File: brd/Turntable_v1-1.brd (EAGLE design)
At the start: 100 x 80 mm, 117 parts, among them CON1 Pannel, CON2 CAN, CON3 Turntable, CON4 STEPPER_CON, CON5 STEPPER_CON, CON8 SPK, IC1 7805, IC2 LM393N, J1 MiniStp2, J10 MiniStp1, Q1 BS170, SW1 EC12E_SW, U2 LED NANO, X1 AK500/2+M, X2 AK500/2+M, X3 MAB 5SH Conrad: 738247 - VQ, X4 AK500/2+M, X5 Reichelt MEBP 8-8S

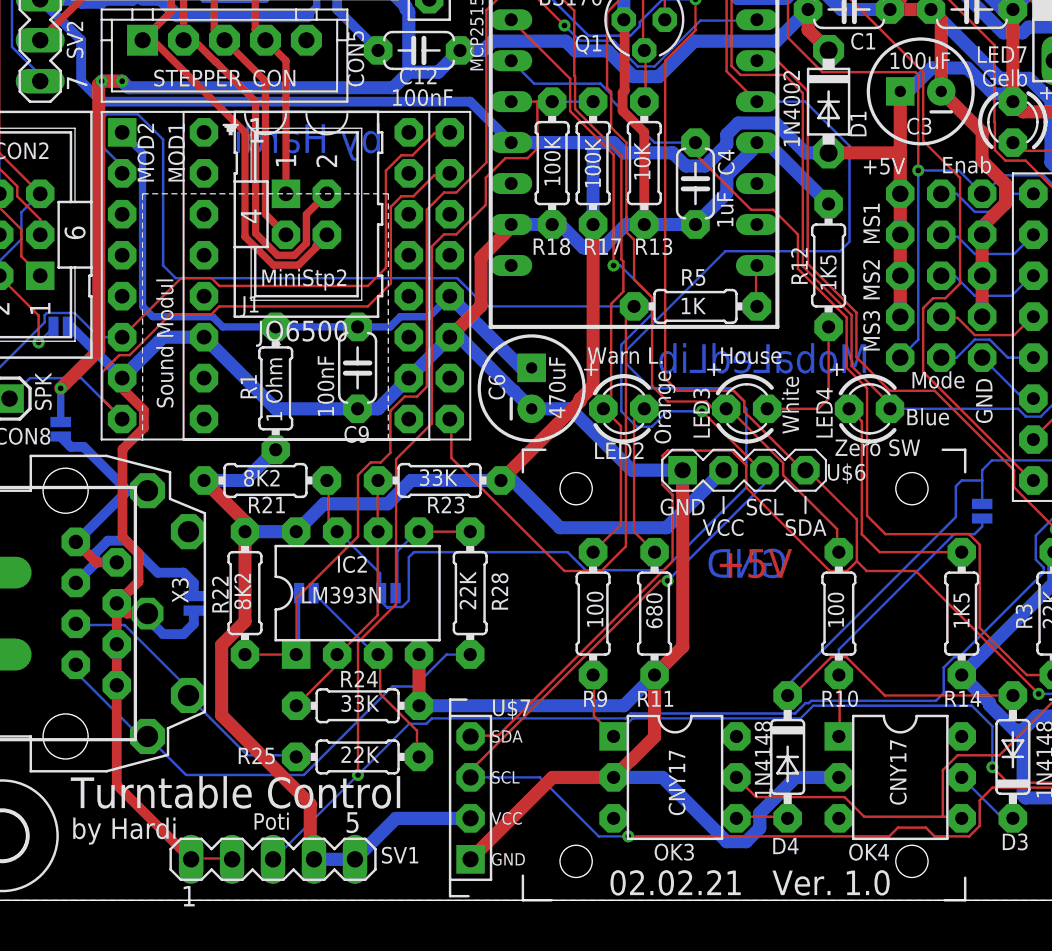
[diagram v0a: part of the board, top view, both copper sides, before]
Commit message: Update 2021-04-12
+ R6 and R7, PullUps for I2C
~ CAN-Modul VCC to +5V
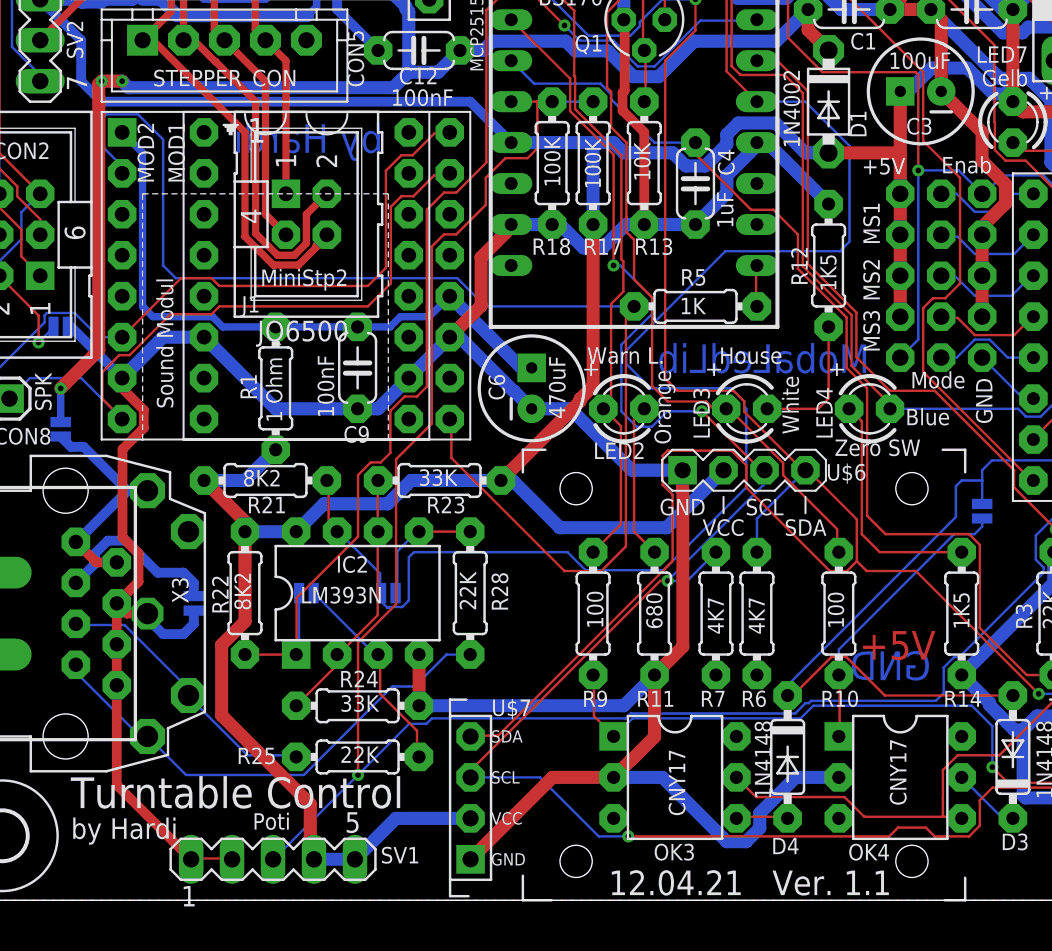
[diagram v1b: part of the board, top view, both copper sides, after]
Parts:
- added R6, R7: 4K7, Sound_MP3-TF-16P_and_WS2811:RCL_0204/7
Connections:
- removed net VCC: CAN1.1
- net +5V: now also CAN1.1, R6.1, R7.1
- net SCL: now also R7.2
- net SDA: now also R6.2
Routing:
- net SDA: track 168.7 -> 175.0 mm
- net SCL: track 162.6 -> 166.3 mm
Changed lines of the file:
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@@
 <?xml version="1.0" encoding="utf-8"?>
 <!DOCTYPE eagle SYSTEM "eagle.dtd">
-<eagle version="9.5.2">
+<eagle version="9.6.2">
 <drawing>
 <settings>
@@
 <setting verticaltext="up"/>
 </settings>
-<grid distance="50" unitdist="mil" unit="mil" style="lines" multiple="1" display="yes" altdistance="12.5" altunitdist="mil" altunit="mil"/>
+<grid distance="12.5" unitdist="mil" unit="mil" style="lines" multiple="1" display="yes" altdistance="12.5" altunitdist="mil" altunit="mil"/>
 <layers>
 <layer number="1" name="Top" color="4" fill="1" visible="yes" active="yes"/>
@@
 <layer number="25" name="tNames" color="7" fill="1" visible="yes" active="yes"/>
 <layer number="26" name="bNames" color="7" fill="1" visible="yes" active="yes"/>
-<layer number="27" name="tValues" color="7" fill="1" visible="no" active="yes"/>
+<layer number="27" name="tValues" color="7" fill="1" visible="yes" active="yes"/>
 <layer number="28" name="bValues" color="7" fill="1" visible="no" active="yes"/>
 <layer number="29" name="tStop" color="7" fill="3" visible="no" active="yes"/>
@@
 <text x="60.96" y="28.575" size="1.016" layer="21" rot="R180">Zero SW</text>
 <text x="45.085" y="34.29" size="1.016" layer="21" rot="R180">Warn L.</text>
-<text x="52.705" y="20.0025" size="1.778" layer="16" font="vector" ratio="12" rot="MR0">GND</text>
-<text x="48.26" y="20.0025" size="1.778" layer="1" font="vector" ratio="12">+5V</text>
+<text x="61.595" y="13.6525" size="1.778" layer="16" font="vector" ratio="12" rot="MR0">GND</text>
+<text x="57.15" y="14.9225" size="1.778" layer="1" font="vector" ratio="12">+5V</text>
 <text x="70.8025" y="4.1275" size="1.016" layer="21">GND</text>
 <text x="74.93" y="4.1275" size="1.016" layer="21">+5V</text>
 </plain>
 <attributes>
-<attribute name="RELEASE_DAY" value="02.02.21"/>
-<attribute name="RELEASE_VER" value="Ver. 1.0"/>
+<attribute name="RELEASE_DAY" value="12.04.21"/>
+<attribute name="RELEASE_VER" value="Ver. 1.1"/>
 </attributes>
 <variantdefs>
@@
 <autorouter>
 <pass name="Default">
-<param name="RoutingGrid" value="50mil"/>
+<param name="RoutingGrid" value="6.25mil"/>
 <param name="AutoGrid" value="1"/>
 <param name="Efforts" value="2"/>
@@
 <element name="JP8" library="adafruit" package="1X03-CLEANBIG" value="Enab" x="27.305" y="64.77" smashed="yes" rot="R90">
 <attribute name="VALUE" x="26.3525" y="63.5" size="0.8128" layer="25" rot="R90"/>
+</element>
+<element name="R6" library="Sound_MP3-TF-16P_and_WS2811" package="RCL_0204/7" value="4K7" x="50.8" y="17.78" smashed="yes" rot="R90">
+<attribute name="NAME" x="51.435" y="12.9921" size="0.9906" layer="25" ratio="10" rot="R180"/>
+<attribute name="SPICEPREFIX" value="R" x="50.8" y="17.78" size="1.778" layer="27" rot="R90" display="off"/>
+<attribute name="VALUE" x="51.2826" y="16.4719" size="0.9906" layer="25" ratio="10" rot="R90"/>
+</element>
+<element name="R7" library="Sound_MP3-TF-16P_and_WS2811" package="RCL_0204/7" value="4K7" x="48.26" y="17.78" smashed="yes" rot="R90">
+<attribute name="NAME" x="48.895" y="12.9921" size="0.9906" layer="25" ratio="10" rot="R180"/>
+<attribute name="SPICEPREFIX" value="R" x="48.26" y="17.78" size="1.778" layer="27" rot="R90" display="off"/>
+<attribute name="VALUE" x="48.7426" y="16.4719" size="0.9906" layer="25" ratio="10" rot="R90"/>
 </element>
 </elements>
@@
 <wire x1="10.16" y1="49.53" x2="8.89" y2="50.8" width="0.6096" layer="16"/>
 <wire x1="8.89" y1="50.8" x2="8.89" y2="53.34" width="0.6096" layer="16"/>
-<wire x1="33.02" y1="49.53" x2="10.16" y2="49.53" width="0.6096" layer="16"/>
+<wire x1="10.16" y1="49.53" x2="33.02" y2="49.53" width="0.6096" layer="16"/>
 <contactref element="SV3" pad="4"/>
 <wire x1="67.31" y1="6.4925" x2="67.4525" y2="6.35" width="0.8128" layer="16"/>
@@
 <wire x1="40.64" y1="46.99" x2="41.91" y2="46.99" width="0.8128" layer="16"/>
 <wire x1="41.91" y1="46.99" x2="42.545" y2="46.355" width="0.8128" layer="16"/>
+<contactref element="R6" pad="1"/>
+<contactref element="R7" pad="1"/>
+<contactref element="CAN1" pad="1"/>
 </signal>
 <signal name="DCC/SX">
@@
 <via x="10.16" y="50.8" extent="1-16" drill="0.35"/>
 </signal>
-<signal name="VCC">
-<contactref element="CAN1" pad="1"/>
-</signal>
 <signal name="N$3">
 <contactref element="CON2" pad="5"/>
@@
 <wire x1="85.75005625" y1="7.4676" x2="84.7852" y2="8.43245625" width="0.1524" layer="16"/>
 <wire x1="88.5444" y1="7.4676" x2="85.75005625" y2="7.4676" width="0.1524" layer="16"/>
+<contactref element="R6" pad="2"/>
+<wire x1="53.81" y1="26.67" x2="50.8" y2="23.66" width="0.1524" layer="16"/>
+<wire x1="50.8" y1="23.66" x2="50.8" y2="21.59" width="0.1524" layer="16"/>
 </signal>
 <signal name="SCL">
@@
 <wire x1="42.3926" y1="30.32186875" x2="42.3926" y2="34.46206875" width="0.1524" layer="16"/>
 <wire x1="44.2976" y1="37.3888" x2="42.3164" y2="39.37" width="0.1524" layer="16"/>
+<contactref element="R7" pad="2"/>
+<wire x1="48.26" y1="21.59" x2="46.482" y2="19.812" width="0.1524" layer="16"/>
+<wire x1="46.482" y1="19.812" x2="45.2628" y2="19.812" width="0.1524" layer="16"/>
 </signal>
 <signal name="POTI">
